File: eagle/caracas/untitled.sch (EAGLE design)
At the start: 8 parts, among them IC1 4027N

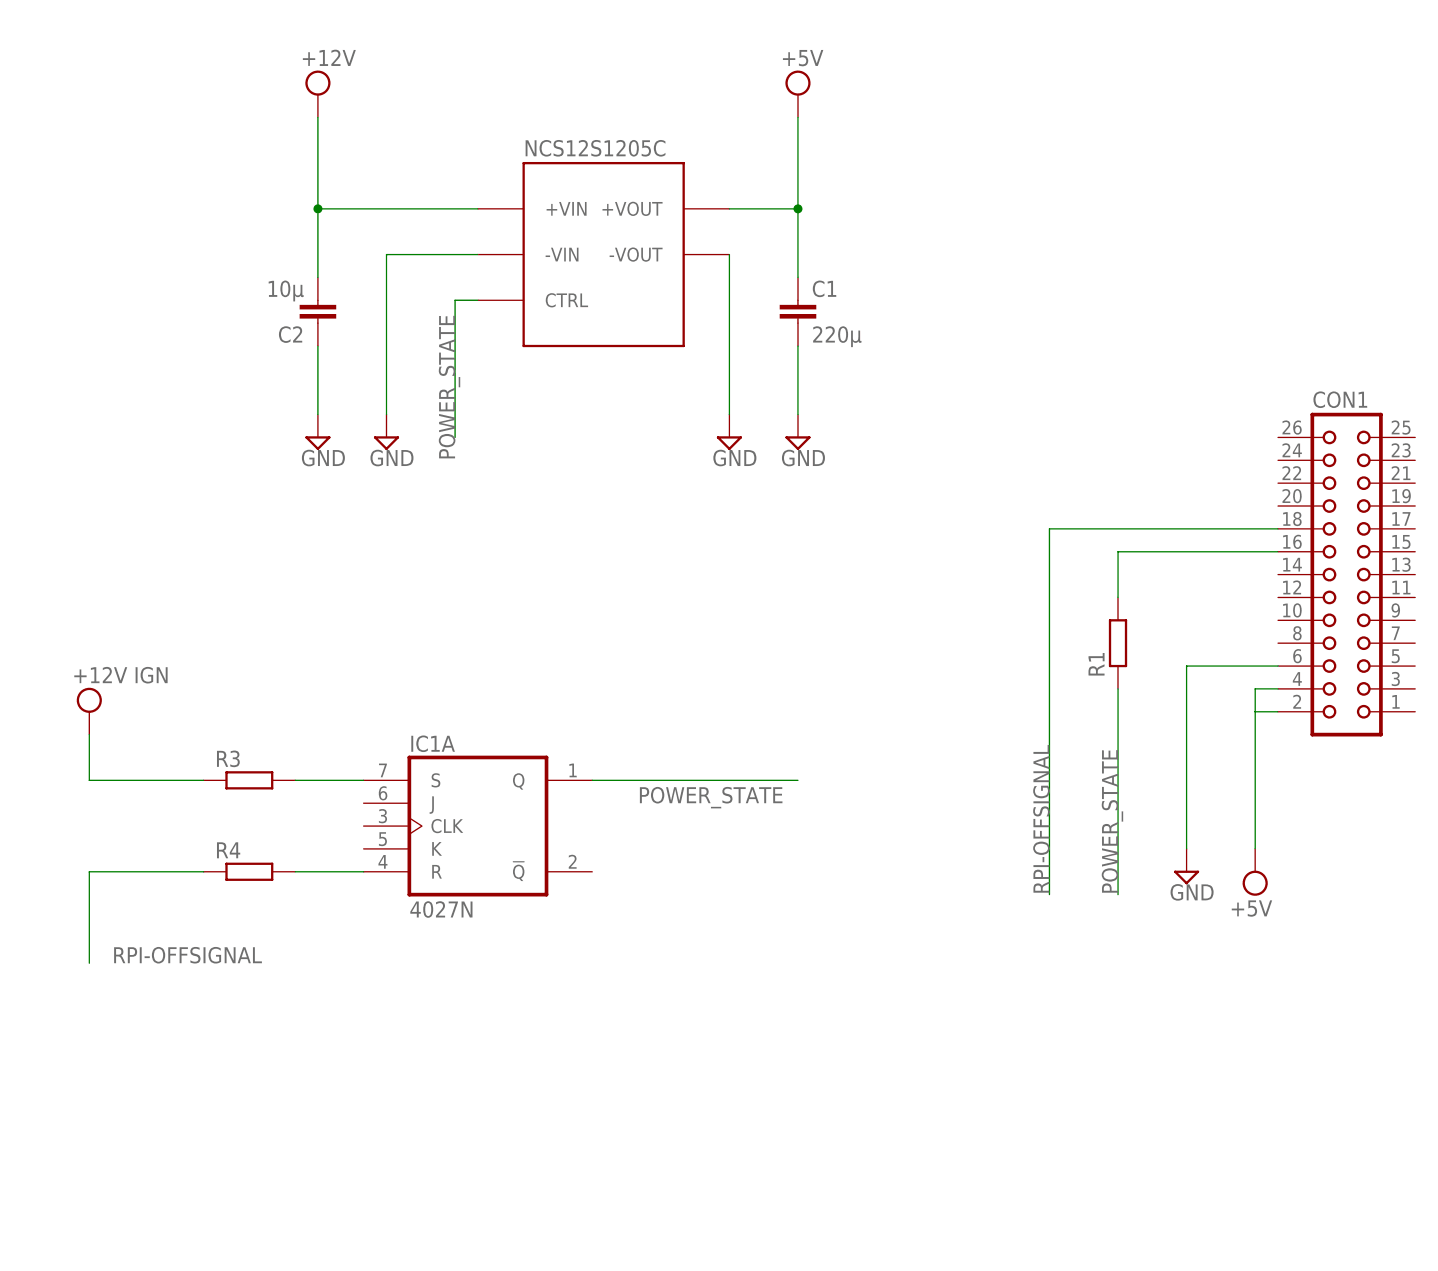
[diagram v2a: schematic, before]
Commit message: EAGLE: draw SATA connector into schematics.
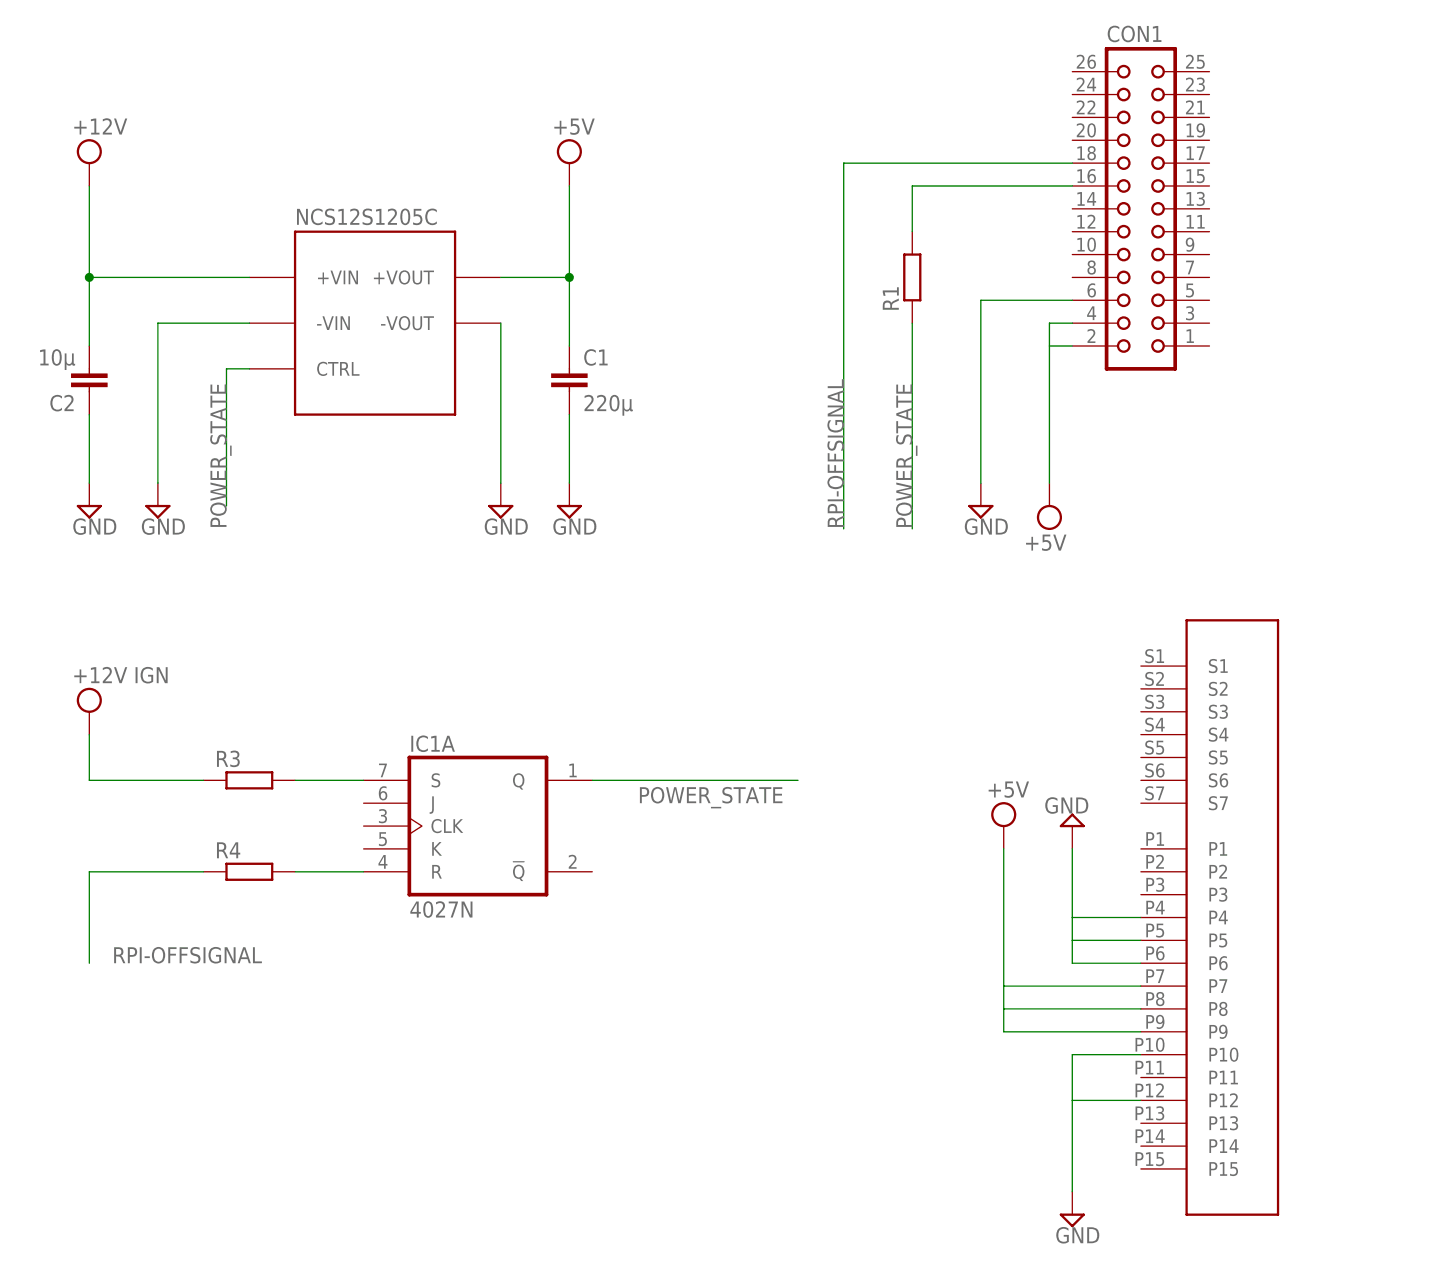
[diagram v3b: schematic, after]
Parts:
- added U$2: CD2109, caracas:CD2109
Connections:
- new net VCC: U$2.P7, U$2.P8, U$2.P9
- net GND: now also U$2.P10, U$2.P12, U$2.P4, U$2.P5, U$2.P6
- net POWER_STATE: now also R1.1
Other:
- moved on the sheet: C1, C2, CON1, R1

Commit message: Finished design?
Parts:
- removed R3, R4: (no value), rcl:R-EU_0207/10
- added U$3: MKDS3, caracas:MKDS3
- R1: value (none) -> 10k
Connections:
- removed net +12V: C2.2, U$1.+VIN
- removed net N$1: IC1A.S, R3.2
- removed net N$2: IC1A.R, R4.2
- net +12V_IGN: now also IC1A.S, U$3G$2.P$1; no longer R3.1
- net +5V: now also U$2.P7, U$2.P8, U$2.P9, U$3G$3.P$1
- net GND: now also IC1A.CLK, IC1A.J, IC1A.K, IC1P.VSS, U$3G$4.P$1
- net RPI-OFFSIGNAL: now also IC1A.R; no longer R4.1
- net VCC: now also C2.2, IC1P.VDD, U$1.+VIN, U$3G$1.P$1; no longer U$2.P7, U$2.P8, U$2.P9
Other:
- moved on the sheet: C1, C2, CON1, IC1A, R1

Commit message: Save the board again.
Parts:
- added R2, R4: 10k, rcl:R-EU_0207/10
- added R3: 86, rcl:R-EU_0207/10
- added T1: 2N2222, transistor:2N2222
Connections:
- new net +12V: T1.C
- new net N$1: IC1A.S
- new net N$2: R3.1, T1.B
- new net N$4: IC1A.R, R4.2, T1.E
- net +12V_IGN: now also R2.2; no longer IC1A.S
- net GND: now also R2.1, R4.1
- net RPI-OFFSIGNAL: now also R3.2; no longer IC1A.R
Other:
- moved on the sheet: C1, C2, CON1, IC1A, IC1P, R1

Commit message: WIP on electronics schematics.
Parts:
- removed C1: 220µ, rcl:C-EU025-024X044
- removed C2: 10µ, rcl:C-EU025-024X044
- removed R3: 86, rcl:R-EU_0207/10
- removed R4: 10k, rcl:R-EU_0207/10
- removed T1: 2N2222, transistor:2N2222
- added Q1: IRFP250, transistor-power:IRFP250
- added R5, R6, R7, R8: (no value), rcl:R-EU_0207/10
- R2: value 10k -> (none)
- U$1: value NCS12S1205C -> MCP3008-I/P; device caracas:NCS12S1205C -> mpc3008:MCP3008-I/P
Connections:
- removed net +12V: T1.C
- removed net N$4: IC1A.R, R4.2, T1.E
- new net +3.3V: IC1P.VDD, R2.2, R5.1
- new net +3.3V1: IC1A.S, R6.2, R7.1
- new net +5V_SW_GND: CON1.6, Q1.D
- net +12V_IGN: now also R6.1; no longer R2.2
- net +5V: now also R2.1; no longer C1.1, U$1.+VOUT
- net GND: now also Q1.S, R5.2, R7.2; no longer C1.2, C2.1, CON1.6, R2.1, R4.1, U$1.-VIN, U$1.-VOUT
- net N$1: now also Q1.G, R8.2; no longer IC1A.S
- net N$2: now also IC1A.!Q; no longer R3.1, T1.B
- net POWER_STATE: now also R8.1; no longer U$1.CTRL
- net RPI-OFFSIGNAL: no longer R3.2
- net VCC: no longer C2.2, IC1P.VDD, U$1.+VIN
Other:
- moved on the sheet: CON1, IC1A, IC1P, R1, R2

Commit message: WIP on electronics schema.
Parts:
- removed R1: 10k, rcl:R-EU_0207/10
- added R3: (no value), rcl:R-EU_0207/10
- added SV1: (no value), con-lsta:FE08-1
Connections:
- net RPI-OFFSIGNAL renamed BUTTON_LEFT
- new net BUTTON_CLICK: CON1.22
- new net BUTTON_RIGHT: CON1.15
- new net N$4: CON1.21, U$1.DOUT
- new net N$5: CON1.19, U$1.DIN
- new net N$6: CON1.24, U$1.~CS/SHDN
- new net N$7: R3.2, SV1.1
- new net N$8: SV1.2
- net +3.3V: now also U$1.VDD, U$1.VREF
- net GND: now also R3.1, U$1.AGND, U$1.DGND
- net N$3: now also CON1.5, U$1.CLK; no longer CON1.16, R1.2
- net POWER_STATE: now also CON1.16; no longer R1.1
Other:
- moved on the sheet: CON1, U$1

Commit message: More WIP on the electronics schematics, closing in...
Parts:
- removed SV1: (no value), con-lsta:FE08-1
- removed U$3: MKDS3, caracas:MKDS3
- added R1, R10, R11, R12, R13, R14, R15, R4, R9: (no value), rcl:R-EU_0207/10
- added X1, X2, X5, X6: 22-23-2021, con-molex:22-23-2021
- added X3, X4: 22-23-2041, con-molex:22-23-2041
- U$2: value CD2109 -> MKDS3; device caracas:CD2109 -> caracas:MKDS3
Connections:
- removed net BUTTON_CLICK: CON1.22
- removed net BUTTON_LEFT: CON1.18
- removed net BUTTON_RIGHT: CON1.15
- new net ANA_0: R8.1, U$1.CH0, X4-3.S
- new net ANA_1: R9.1, U$1.CH1, X4-2.S
- new net N$10: CON1.12, R13.1, X3-2.S
- new net N$11: IC1B.!Q, R11.2
- new net N$12: IC1B.CLK, IC1B.J, IC1B.K, IC1B.R, IC1B.S, R10.2
- new net N$13: IC1B.Q, R12.2
- new net N$9: IC1A.CLK, IC1A.J, IC1A.K, R6.2
- new net SUICIDE: CON1.11, IC1A.R
- net +12V_IGN: now also R2.1, U$2G$3.P$1; no longer R6.1, U$3G$2.P$1
- net +3.3V: now also R1.2, R4.1, R8.2, R9.2, X3-1.S, X4-4.S; no longer R2.2, R5.1
- net +3.3V1: now also R2.2, R5.1; no longer R6.2, R7.1
- net +5V: now also R1.1, X1-1.S, X1-2.S; no longer R2.1, U$2.P7, U$2.P8, U$2.P9, U$3G$3.P$1
- net GND: now also R10.1, R11.1, R12.1, R13.2, R14.2, R15.2, R4.2, R6.1, R7.1, U$2G$1.P$1, X4-1.S, X5-1.S, X5-2.S, X6-1.S, X6-2.S; no longer IC1A.CLK, IC1A.J, IC1A.K, R3.1, R7.2, U$2.P10, U$2.P12, U$2.P4, U$2.P5, U$2.P6, U$3G$4.P$1
- net N$1: now also R3.2; no longer R8.2
- net N$2: now also R7.2
- net N$7: now also CON1.8, R15.1, X3-4.S; no longer R3.2, SV1.1
- net N$8: now also CON1.10, R14.1, X3-3.S; no longer SV1.2
- net POWER_STATE: now also R3.1; no longer R8.1
- net VCC: now also U$2G$2.P$1, X2-1.S, X2-2.S; no longer U$3G$1.P$1
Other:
- moved on the sheet: CON1, IC1A, IC1P, Q1, R2, R3, R5, R6, R7, R8, U$1
